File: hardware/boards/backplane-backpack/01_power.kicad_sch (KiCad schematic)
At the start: 28 parts, among them J1 VIN INPUT (TBD), U4 LMR51610YDBVR, U5 LMR51610YDBVR

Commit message: chore: checkpoint workspace changes
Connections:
- net GND: now also J1.1 (Pin_1); no longer J1.2 (Pin_2)
- net VIN_RAW: now also J1.2 (Pin_2); no longer J1.1 (Pin_1)
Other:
- company: (none) -> Karl Quinsland
- title: Power Entry and Regulators -> Backplane Backpack
- moved on the sheet: J1

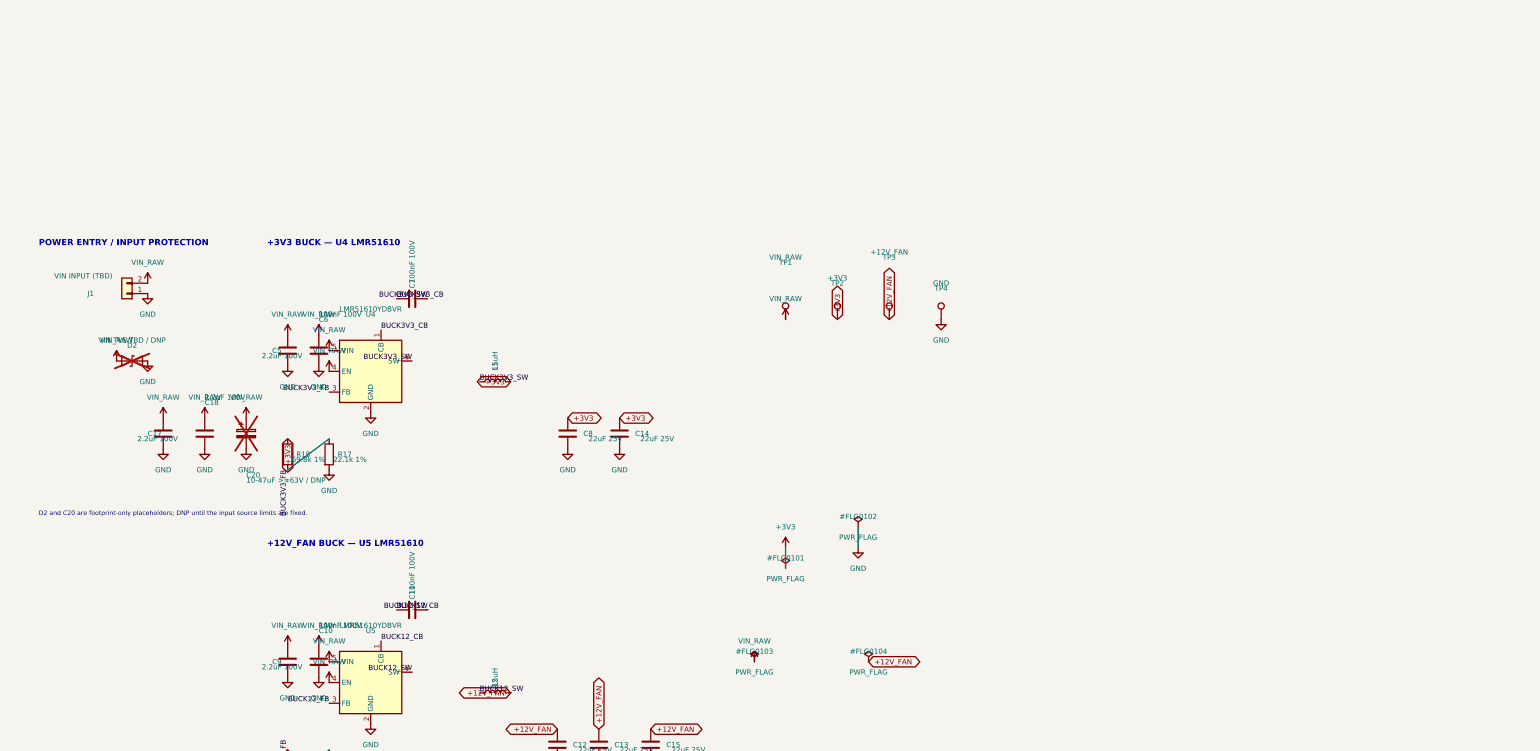
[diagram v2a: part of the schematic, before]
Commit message: fix: standardize +3V3 power symbols
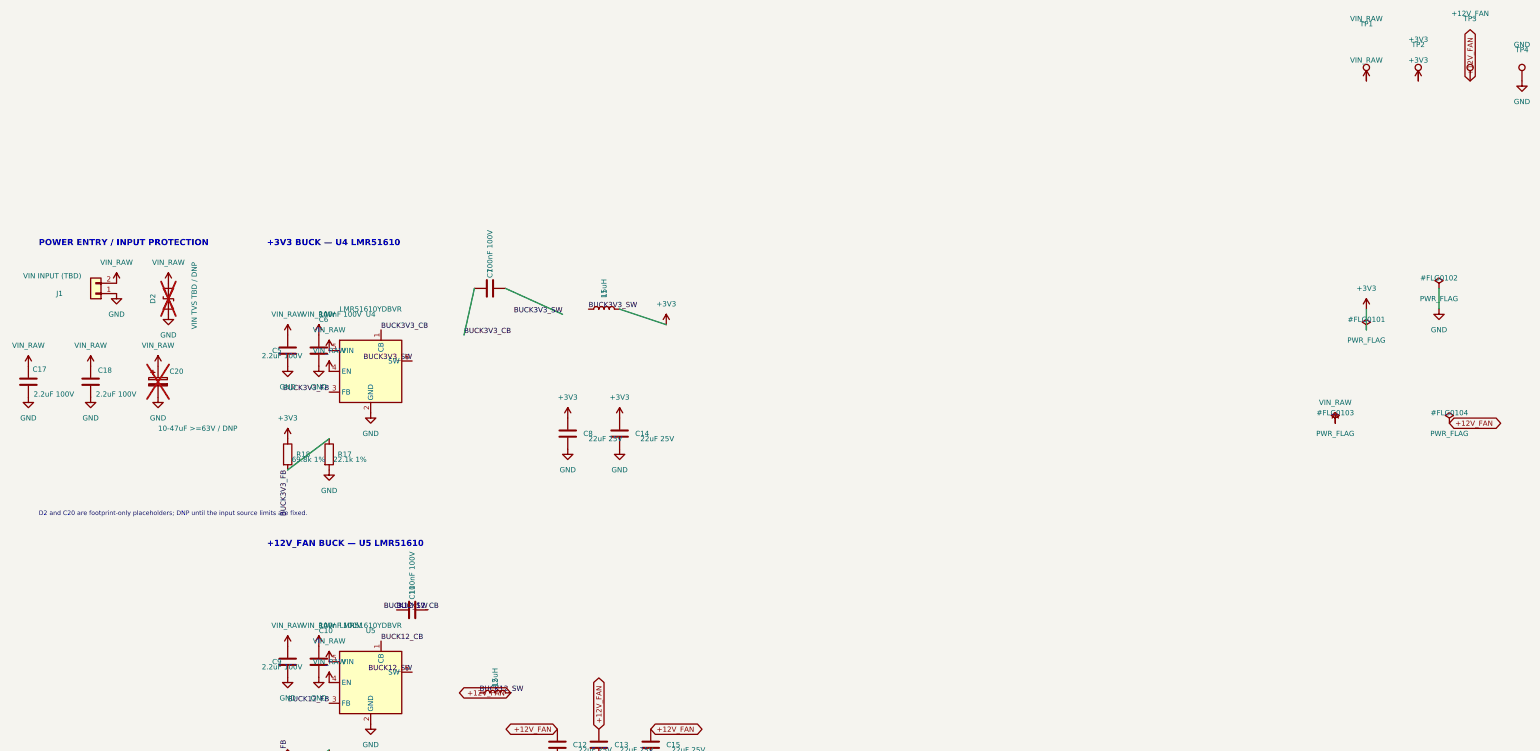
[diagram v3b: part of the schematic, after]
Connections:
- net GND: now also D2.1 (A1); no longer D2.2 (A2)
- net VIN_RAW: now also D2.2 (A2); no longer D2.1 (A1)
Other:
- moved on the sheet: C17, C18, C20, C7, J1, L1, TP1, TP2, TP3, TP4

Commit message: chore: checkpoint buck layout changes
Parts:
- C20: value 10-47uF >=63V / DNP -> 10-47uF >=63V
- D2: value VIN TVS TBD / DNP -> VIN TVS TBD
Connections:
- net +12V_FAN: no longer C12.1, C13.1, C15.1
- net BUCK3V3_CB: now also C7.2; no longer C7.1
- net BUCK3V3_FB: no longer names the net of R17.1, R18.2, U4.3 (FB)
- net BUCK3V3_SW: no longer names the net of L1.1, U4.6 (SW)
- net BUCK3V3_SW: now also C7.1; no longer C7.2
- new net +12V: C12.1, C13.1, C15.1
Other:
- note added: "+3V3 BUCK"
- note removed: "+3V3 BUCK — U4 LMR51610"
- moved on the sheet: C11, C13, C14, C15, C5, C6, C8, L1, L2, R17, R18, R19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

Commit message: fix: standardize 12V rail and mirror buck layout
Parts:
- TP3: value +12V_FAN -> +12V
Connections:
- net +12V_FAN is gone; now on net +12V: L2.2, R20.1, TP3.1
- net BUCK12_CB: now also C11.2; no longer C11.1
- net BUCK12_FB: no longer names the net of R19.1, R20.2, U5.3 (FB)
- net BUCK12_SW: no longer names the net of L2.1, U5.6 (SW)
- net BUCK12_SW: now also C11.1; no longer C11.2
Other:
- note added: "+12V BUCK"
- note removed: "+12V_FAN BUCK — U5 LMR51610"
- moved on the sheet: C10, C11, C12, C13, C15, C9, L2, R19, R20, U5

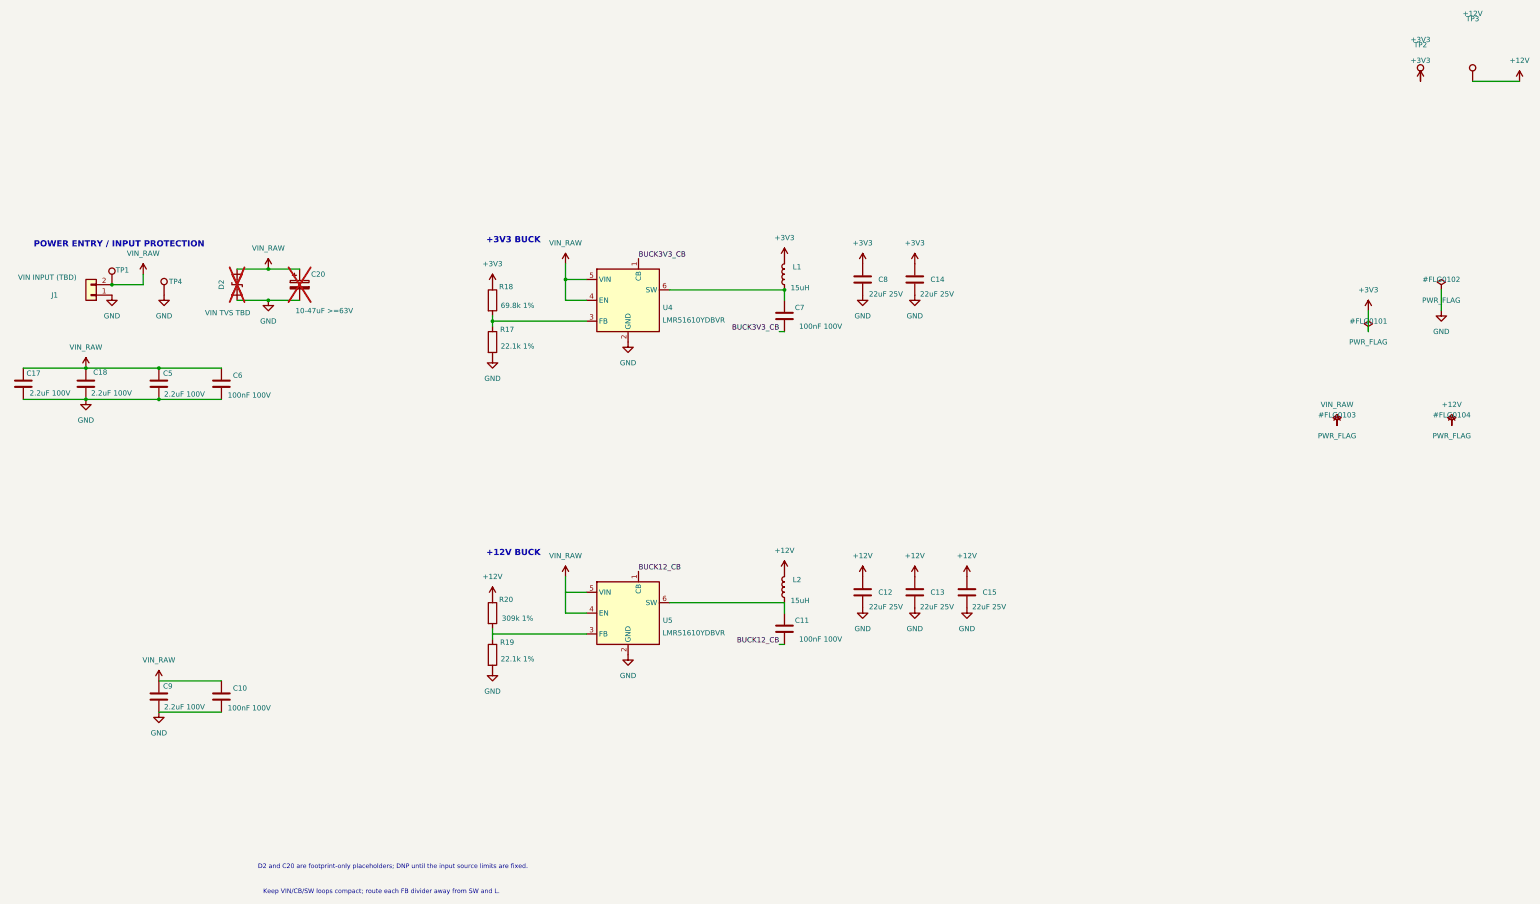
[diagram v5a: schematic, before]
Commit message: fix: restore and align buck regulator stages
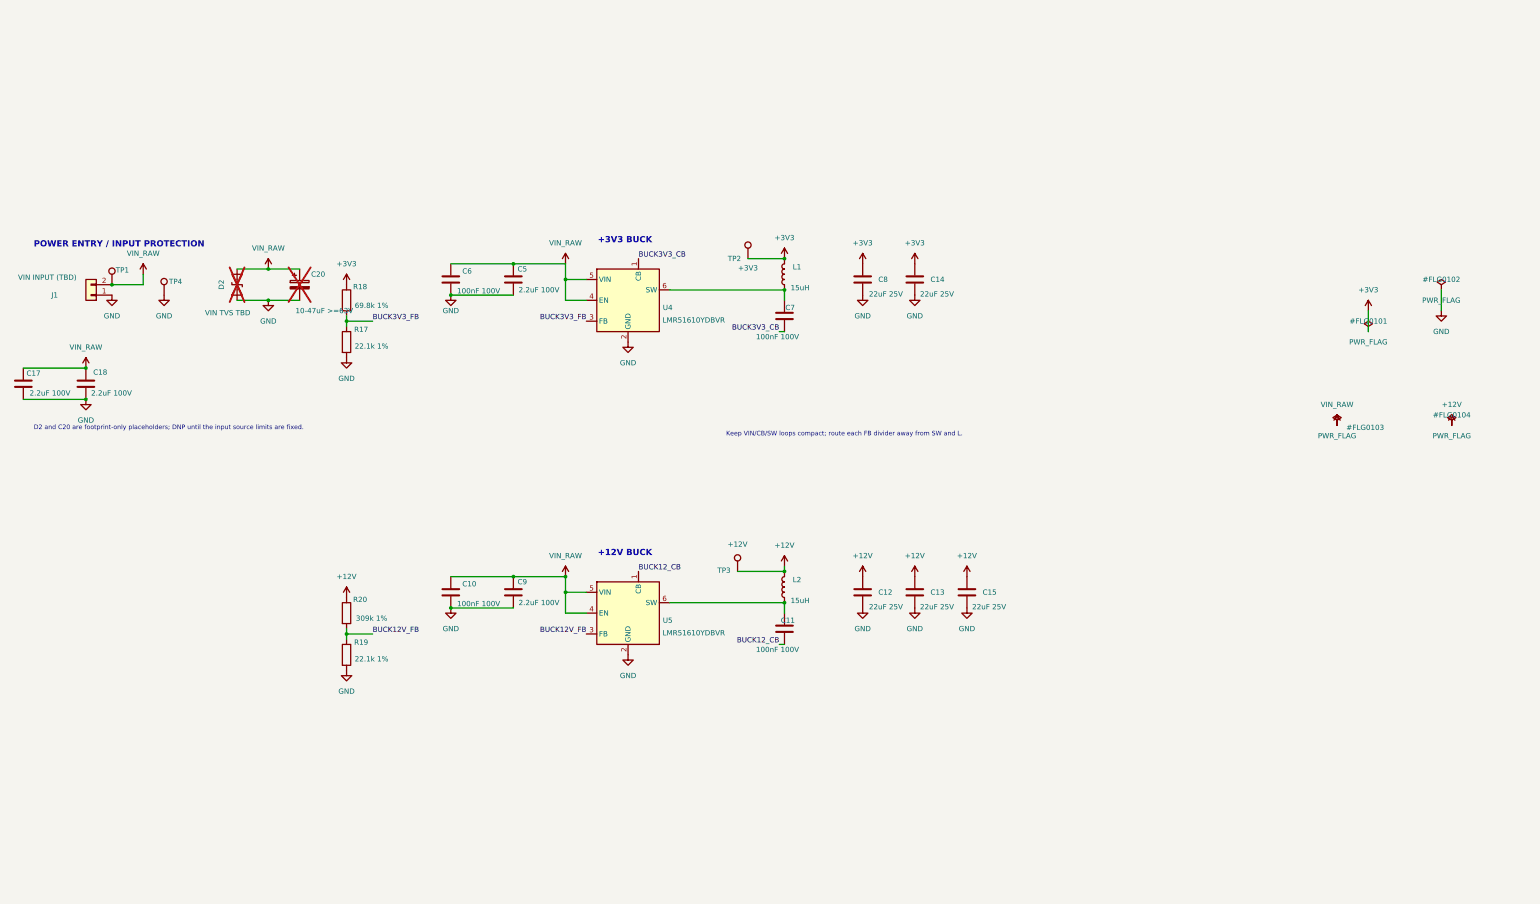
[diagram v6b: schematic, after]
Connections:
- net BUCK12_CB: now also C11.1; no longer C11.2
- net BUCK3V3_CB: now also C7.1; no longer C7.2
- net BUCK12V_FB: now reaches R19.1, R20.2, U5.3 (FB)
- net at L2.1, U5.6 (SW): now also C11.2; no longer C11.1
- net BUCK3V3_FB: now reaches R17.1, R18.2, U4.3 (FB)
- net at L1.1, U4.6 (SW): now also C7.2; no longer C7.1
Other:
- moved on the sheet: C11, C7, R17, R18, R19, R20, TP3

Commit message: chore: checkpoint workspace changes
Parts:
- added H1, H2, H3, H4, H5, H6: MountingHole_Pad, MountingHole:MountingHole_2.2mm_M2_Pad_Via, symbol Mechanical:MountingHole_Pad
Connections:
- net GND: now also H1.1, H2.1, H3.1, H4.1, H5.1, H6.1
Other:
- note added: "Mechanical/Mount"
- note added: "Power testpoints"
- moved on the sheet: C14, C5, C6, C7, C8, L1, R17, R18, U4

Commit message: chore: checkpoint current design changes
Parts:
- removed J1: VIN INPUT (TBD), symbol Connector_Generic:Conn_01x02
- added J1: DC_IN, mini-rack-power:DEGSON_DG135T-10.16-02P, symbol Connector:Screw_Terminal_01x02
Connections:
- net GND: now also J1.1 (Pin_1)
- net VIN_RAW: now also J1.2 (Pin_2)
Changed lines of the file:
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@@
 	)
 	(symbol
-		(lib_id "Connector_Generic:Conn_01x02")
-		(at 34.29 29.21 180)
-		(unit 1)
-		(body_style 1)
-		(exclude_from_sim no)
-		(in_bom yes)
-		(on_board yes)
-		(in_pos_files yes)
-		(dnp no)
-		(property "Reference" "J1"
-			(at 25.4 29.21 0)
-			(show_name no)
-			(do_not_autoplace no)
-			(effects
-				(font
-					(size 1.27 1.27)
-				)
-			)
-		)
-		(property "Value" "VIN INPUT (TBD)"
-			(at 23.622 24.892 0)
-			(show_name no)
-			(do_not_autoplace no)
-			(effects
-				(font
-					(size 1.27 1.27)
-				)
-			)
-		)
-		(property "Footprint" ""
-			(at 34.29 29.21 0)
-			(hide yes)
-			(show_name no)
-			(do_not_autoplace no)
-			(effects
-				(font
-					(size 1.27 1.27)
-				)
-			)
-		)
-		(property "Datasheet" ""
-			(at 34.29 29.21 0)
-			(hide yes)
-			(show_name no)
-			(do_not_autoplace no)
-			(effects
-				(font
-					(size 1.27 1.27)
-				)
-			)
-		)
-		(property "Description" "Generic connector, single row, 01x02, script generated (kicad-library-utils/schlib/autogen/connector/)"
-			(at 34.29 29.21 0)
-			(hide yes)
-			(show_name no)
-			(do_not_autoplace no)
-			(effects
-				(font
-					(size 1.27 1.27)
-				)
-			)
-		)
-		(property "MPN" "C1206X225K101T"
-			(at 34.29 29.21 0)
-			(hide yes)
-			(show_name no)
-			(do_not_autoplace no)
-			(effects
-				(font
-					(size 1.27 1.27)
-				)
-			)
-		)
-		(property "LCSC" "C106051"
-			(at 34.29 29.21 0)
-			(hide yes)
-			(show_name no)
-			(do_not_autoplace no)
-			(effects
-				(font
-					(size 1.27 1.27)
-				)
-			)
-		)
-		(property "Package" "1206"
-			(at 34.29 29.21 0)
-			(hide yes)
-			(show_name no)
-			(do_not_autoplace no)
-			(effects
-				(font
-					(size 1.27 1.27)
-				)
-			)
-		)
-		(property "Population" "POP"
-			(at 34.29 29.21 0)
-			(hide yes)
-			(show_name no)
-			(do_not_autoplace no)
-			(effects
-				(font
-					(size 1.27 1.27)
-				)
-			)
-		)
-		(pin "1"
-		)
-		(pin "2"
-		)
-		(instances
-			(project "backplane-prototype-mate"
-				(path "/60406afc-75de-47dd-afde-497547cd0d52"
-					(reference "J1")
-					(unit 1)
-				)
-			)
-			(project "backplane-backpack"
-				(path "/76314aad-fff2-4237-8c4a-2dbd4e06a2e1/762a1ab9-bdaa-41f1-9da1-1687126e729c"
-					(reference "J1")
-					(unit 1)
-				)
-			)
-		)
-	)
-	(symbol
 		(lib_id "power:+12V")
 		(at 96.52 102.87 0)
@@
 					(unit 1)
 				)
+			)
+		)
+	)
+	(symbol
+		(lib_id "Connector:Screw_Terminal_01x02")
+		(at 34.29 29.21 180)
+		(unit 1)
+		(body_style 1)
+		(exclude_from_sim no)
+		(in_bom yes)
+		(on_board yes)
+		(in_pos_files yes)
+		(dnp no)
+		(property "Reference" "J1"
+			(at 28.702 21.844 0)
+			(show_name no)
+			(do_not_autoplace no)
+			(effects
+				(font
+					(size 1.27 1.27)
+				)
+			)
+		)
+		(property "Value" "DC_IN"
+			(at 29.21 24.638 0)
+			(show_name no)
+			(do_not_autoplace no)
+			(effects
+				(font
+					(size 1.27 1.27)
+				)
+			)
+		)
+		(property "Footprint" "mini-rack-power:DEGSON_DG135T-10.16-02P"
+			(at 34.29 29.21 0)
+			(hide yes)
+			(show_name no)
+			(do_not_autoplace no)
+			(effects
+				(font
+					(size 1.27 1.27)
+				)
+			)
+		)
+		(property "Datasheet" ""
+			(at 34.29 29.21 0)
+			(hide yes)
+			(show_name no)
+			(do_not_autoplace no)
+			(effects
+				(font
+					(size 1.27 1.27)
+				)
+			)
+		)
+		(property "Description" "Prototype main DC input screw terminal"
+			(at 34.29 29.21 0)
+			(hide yes)
+			(show_name no)
+			(do_not_autoplace no)
+			(effects
+				(font
+					(size 1.27 1.27)
+				)
+			)
+		)
+		(property "Pinout" "1=GND; 2=+24V"
+			(at 34.29 29.21 0)
+			(hide yes)
+			(show_name no)
+			(do_not_autoplace no)
+			(effects
+				(font
+					(size 1.27 1.27)
+				)
+			)
+		)
+		(pin "1"
+		)
+		(pin "2"
+		)
+		(instances
+			(project "backplane-backpack"
+				(path "/76314aad-fff2-4237-8c4a-2dbd4e06a2e1/762a1ab9-bdaa-41f1-9da1-1687126e729c"
+					(reference "J1")
+					(unit 1)
+				)
